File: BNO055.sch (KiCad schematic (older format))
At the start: 13 parts, among them SW2 SW_Push, U3 BNO055, Y2 32.768kHz

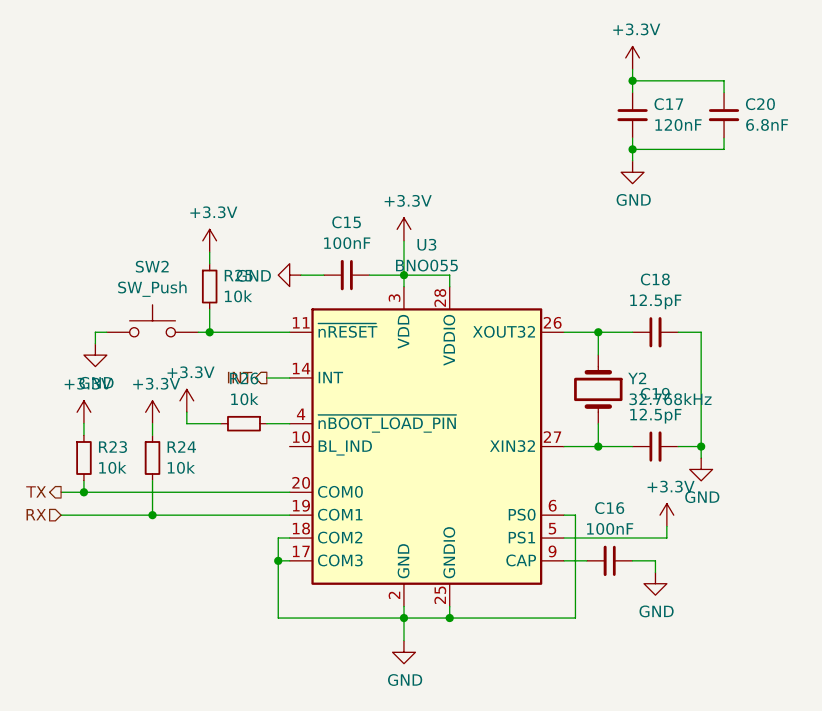
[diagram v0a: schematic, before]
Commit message: LMZM23600 from official kicad lib
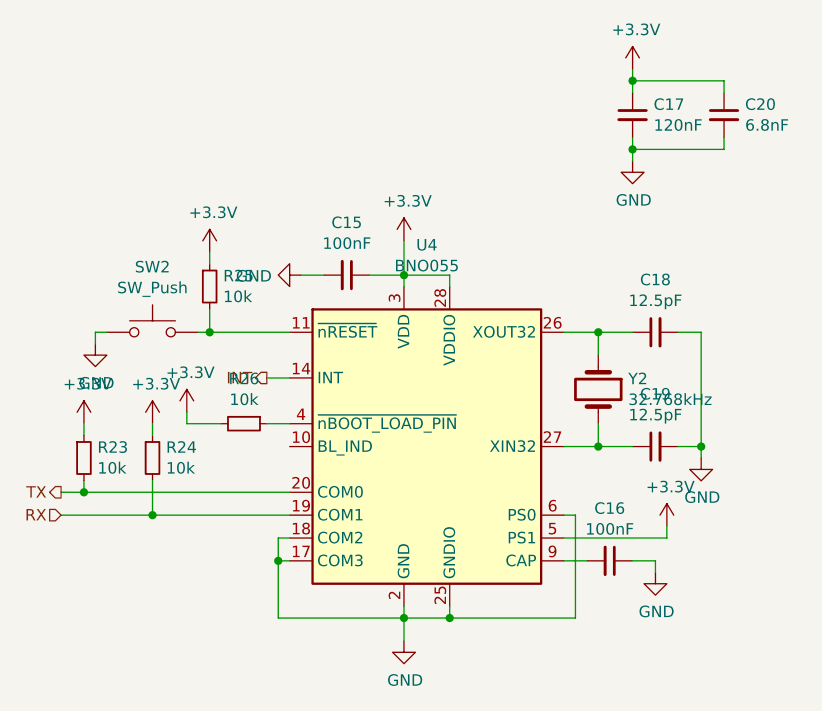
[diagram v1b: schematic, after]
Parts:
- renumbered U3 to U4
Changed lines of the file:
@@
 $EndDescr
 $Comp
-L Sensor_Motion:BNO055 U3
+L Sensor_Motion:BNO055 U4
 U 1 1 5C912A06
 P 6050 3250
-F 0 "U3" H 6050 4131 50  0000 C CNN
+F 0 "U4" H 6050 4131 50  0000 C CNN
 F 1 "BNO055" H 6050 4040 50  0000 C CNN
 F 2 "Package_LGA:LGA-28_5.2x3.8mm_P0.5mm" H 6300 2600 50  0001 L CNN

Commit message: use submodule for FT230
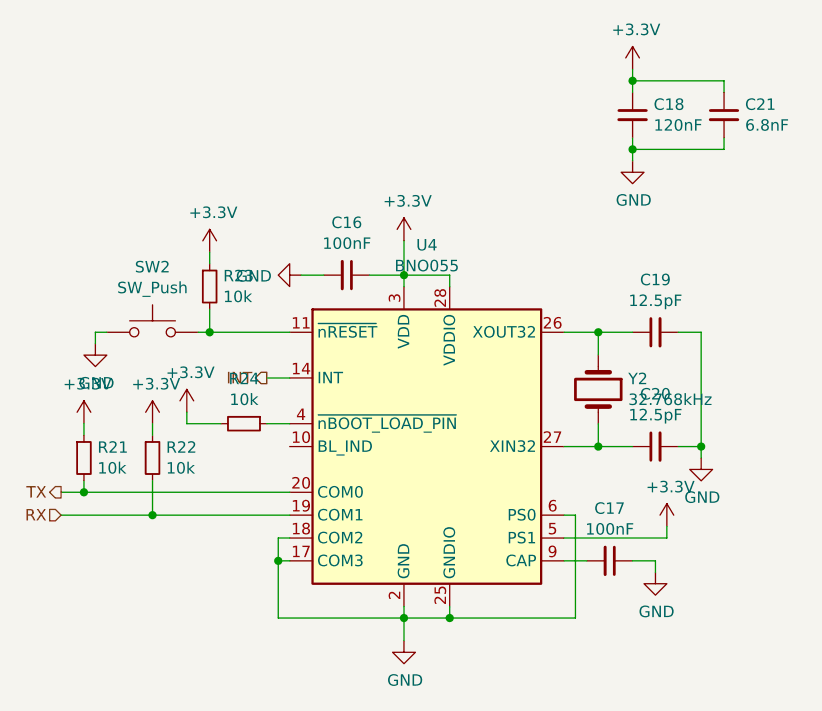
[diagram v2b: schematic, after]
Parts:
- renumbered C15 to C16, C16 to C17, C17 to C18, C18 to C19, C19 to C20, C20 to C21, R23 to R21, R24 to R22, R25 to R23, R26 to R24
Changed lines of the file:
@@
 	5950 4000 5950 4100
 $Comp
-L Device:R_Small R26
+L Device:R_Small R24
 U 1 1 5C915151
 P 5250 3150
-F 0 "R26" V 5054 3150 50  0000 C CNN
+F 0 "R24" V 5054 3150 50  0000 C CNN
 F 1 "10k" V 5145 3150 50  0000 C CNN
 F 2 "Resistor_SMD:R_0603_1608Metric" H 5250 3150 50  0001 C CNN
@@
 	6650 3750 6750 3750
 $Comp
-L Device:C_Small C16
+L Device:C_Small C17
 U 1 1 5C917F1C
 P 6850 3750
-F 0 "C16" V 6621 3750 50  0000 C CNN
+F 0 "C17" V 6621 3750 50  0000 C CNN
 F 1 "100nF" V 6712 3750 50  0000 C CNN
 F 2 "Capacitor_SMD:C_0603_1608Metric" H 6850 3750 50  0001 C CNN
@@
 $EndComp
 $Comp
-L Device:C_Small C15
+L Device:C_Small C16
 U 1 1 5C9184D6
 P 5700 2500
-F 0 "C15" V 5471 2500 50  0000 C CNN
+F 0 "C16" V 5471 2500 50  0000 C CNN
 F 1 "100nF" V 5562 2500 50  0000 C CNN
 F 2 "Capacitor_SMD:C_0603_1608Metric" H 5700 2500 50  0001 C CNN
@@
 $EndComp
 $Comp
-L Device:C_Small C17
+L Device:C_Small C18
 U 1 1 5C9161DD
 P 6950 1800
-F 0 "C17" H 7042 1846 50  0000 L CNN
+F 0 "C18" H 7042 1846 50  0000 L CNN
 F 1 "120nF" H 7042 1755 50  0000 L CNN
 F 2 "Capacitor_SMD:C_0603_1608Metric" H 6950 1800 50  0001 C CNN
@@
 $EndComp
 $Comp
-L Device:C_Small C20
+L Device:C_Small C21
 U 1 1 5C91667F
 P 7350 1800
-F 0 "C20" H 7442 1846 50  0000 L CNN
+F 0 "C21" H 7442 1846 50  0000 L CNN
 F 1 "6.8nF" H 7442 1755 50  0000 L CNN
 F 2 "Capacitor_SMD:C_0603_1608Metric" H 7350 1800 50  0001 C CNN
@@
 Connection ~ 6800 2750
 $Comp
-L Device:C_Small C18
+L Device:C_Small C19
 U 1 1 5C91C8F7
 P 7050 2750
-F 0 "C18" V 7279 2750 50  0000 C CNN
+F 0 "C19" V 7279 2750 50  0000 C CNN
 F 1 "12.5pF" V 7188 2750 50  0000 C CNN
 F 2 "Capacitor_SMD:C_0603_1608Metric" H 7050 2750 50  0001 C CNN
@@
 $EndComp
 $Comp
-L Device:C_Small C19
+L Device:C_Small C20
 U 1 1 5C91D1A5
 P 7050 3250
-F 0 "C19" V 7279 3250 50  0000 C CNN
+F 0 "C20" V 7279 3250 50  0000 C CNN
 F 1 "12.5pF" V 7188 3250 50  0000 C CNN
 F 2 "Capacitor_SMD:C_0603_1608Metric" H 7050 3250 50  0001 C CNN
@@
 	5050 2750 5100 2750
 $Comp
-L Device:R_Small R25
+L Device:R_Small R23
 U 1 1 5C99602E
 P 5100 2550
-F 0 "R25" H 5159 2596 50  0000 L CNN
+F 0 "R23" H 5159 2596 50  0000 L CNN
 F 1 "10k" H 5159 2505 50  0000 L CNN
 F 2 "Resistor_SMD:R_0603_1608Metric" H 5100 2550 50  0001 C CNN
@@
 $EndComp
 $Comp
-L Device:R_Small R24
+L Device:R_Small R22
 U 1 1 5C987F45
 P 4850 3300
-F 0 "R24" H 4909 3346 50  0000 L CNN
+F 0 "R22" H 4909 3346 50  0000 L CNN
 F 1 "10k" H 4909 3255 50  0000 L CNN
 F 2 "Resistor_SMD:R_0603_1608Metric" H 4850 3300 50  0001 C CNN
@@
 $EndComp
 $Comp
-L Device:R_Small R23
+L Device:R_Small R21
 U 1 1 5C98871D
 P 4550 3300
-F 0 "R23" H 4609 3346 50  0000 L CNN
+F 0 "R21" H 4609 3346 50  0000 L CNN
 F 1 "10k" H 4609 3255 50  0000 L CNN
 F 2 "Resistor_SMD:R_0603_1608Metric" H 4550 3300 50  0001 C CNN

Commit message: pullups, jumpers
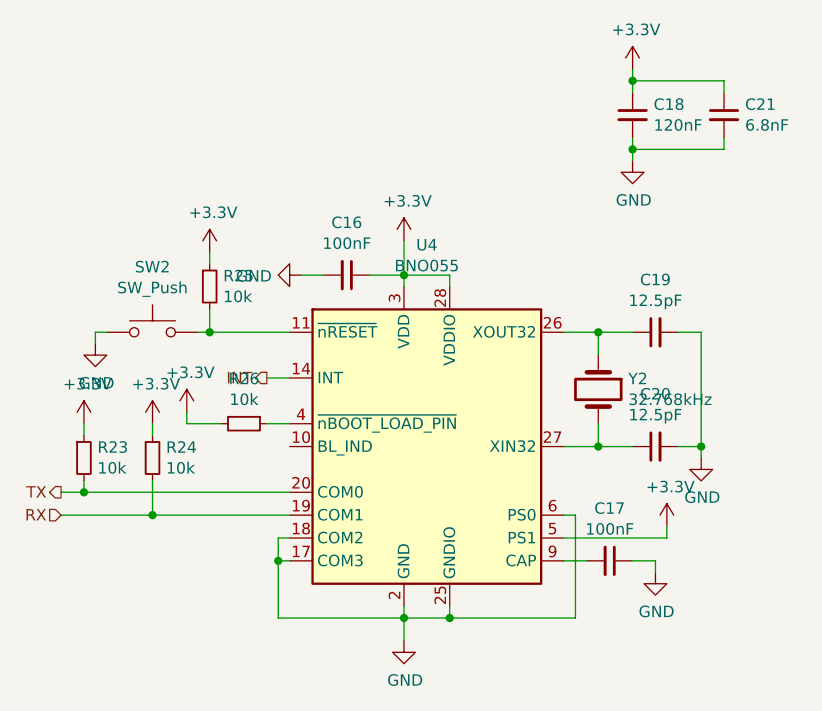
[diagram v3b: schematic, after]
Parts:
- renumbered R21 to R23, R22 to R24, R23 to R25, R24 to R26
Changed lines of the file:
@@
 	5950 4000 5950 4100
 $Comp
-L Device:R_Small R24
+L Device:R_Small R26
 U 1 1 5C915151
 P 5250 3150
-F 0 "R24" V 5054 3150 50  0000 C CNN
+F 0 "R26" V 5054 3150 50  0000 C CNN
 F 1 "10k" V 5145 3150 50  0000 C CNN
 F 2 "Resistor_SMD:R_0603_1608Metric" H 5250 3150 50  0001 C CNN
@@
 	5050 2750 5100 2750
 $Comp
-L Device:R_Small R23
+L Device:R_Small R25
 U 1 1 5C99602E
 P 5100 2550
-F 0 "R23" H 5159 2596 50  0000 L CNN
+F 0 "R25" H 5159 2596 50  0000 L CNN
 F 1 "10k" H 5159 2505 50  0000 L CNN
 F 2 "Resistor_SMD:R_0603_1608Metric" H 5100 2550 50  0001 C CNN
@@
 $EndComp
 $Comp
-L Device:R_Small R22
+L Device:R_Small R24
 U 1 1 5C987F45
 P 4850 3300
-F 0 "R22" H 4909 3346 50  0000 L CNN
+F 0 "R24" H 4909 3346 50  0000 L CNN
 F 1 "10k" H 4909 3255 50  0000 L CNN
 F 2 "Resistor_SMD:R_0603_1608Metric" H 4850 3300 50  0001 C CNN
@@
 $EndComp
 $Comp
-L Device:R_Small R21
+L Device:R_Small R23
 U 1 1 5C98871D
 P 4550 3300
-F 0 "R21" H 4609 3346 50  0000 L CNN
+F 0 "R23" H 4609 3346 50  0000 L CNN
 F 1 "10k" H 4609 3255 50  0000 L CNN
 F 2 "Resistor_SMD:R_0603_1608Metric" H 4550 3300 50  0001 C CNN

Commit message: layout
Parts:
- removed SW2: SW_Push, Button_Switch_SMD:SW_SPST_PTS810, symbol Switch:SW_Push
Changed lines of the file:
@@
 $EndComp
-$Comp
-L Switch:SW_Push SW?
-U 1 1 5C994ABC
-P 4850 2750
-AR Path="/5C8FB8FD/5C994ABC" Ref="SW?"  Part="1"
-AR Path="/5C9128F0/5C994ABC" Ref="SW2"  Part="1"
-F 0 "SW2" H 4850 3035 50  0000 C CNN
-F 1 "SW_Push" H 4850 2944 50  0000 C CNN
-F 2 "Button_Switch_SMD:SW_SPST_PTS810" H 4850 2950 50  0001 C CNN
-F 3 "~" H 4850 2950 50  0001 C CNN
-	1    4850 2750
-	1    0    0    -1
-$EndComp
-Wire Wire Line
-	4650 2750 4600 2750
-Wire Wire Line
-	4600 2750 4600 2800
-$Comp
-L power:GND #PWR?
-U 1 1 5C994AC5
-P 4600 2800
-AR Path="/5C8FB8FD/5C994AC5" Ref="#PWR?"  Part="1"
-AR Path="/5C9128F0/5C994AC5" Ref="#PWR043"  Part="1"
-F 0 "#PWR043" H 4600 2550 50  0001 C CNN
-F 1 "GND" H 4605 2627 50  0000 C CNN
-F 2 "" H 4600 2800 50  0001 C CNN
-F 3 "" H 4600 2800 50  0001 C CNN
-	1    4600 2800
-	1    0    0    -1
-$EndComp
-Wire Wire Line
-	5050 2750 5100 2750
 $Comp
 L Device:R_Small R25
@@
 Wire Wire Line
 	5100 2650 5100 2750
-Connection ~ 5100 2750
 Wire Wire Line
 	5100 2750 5450 2750

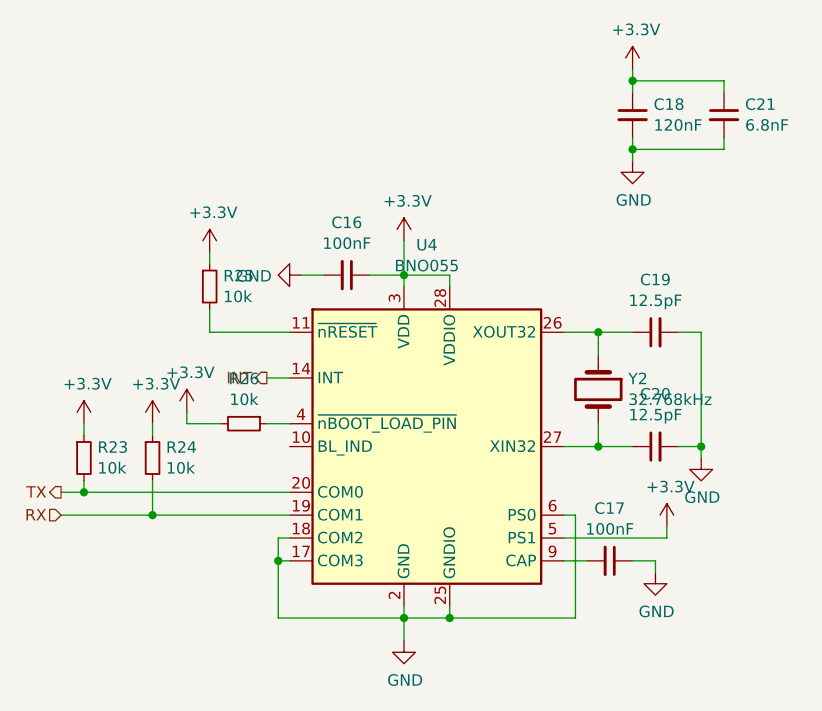
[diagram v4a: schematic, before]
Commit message: small layout fixes
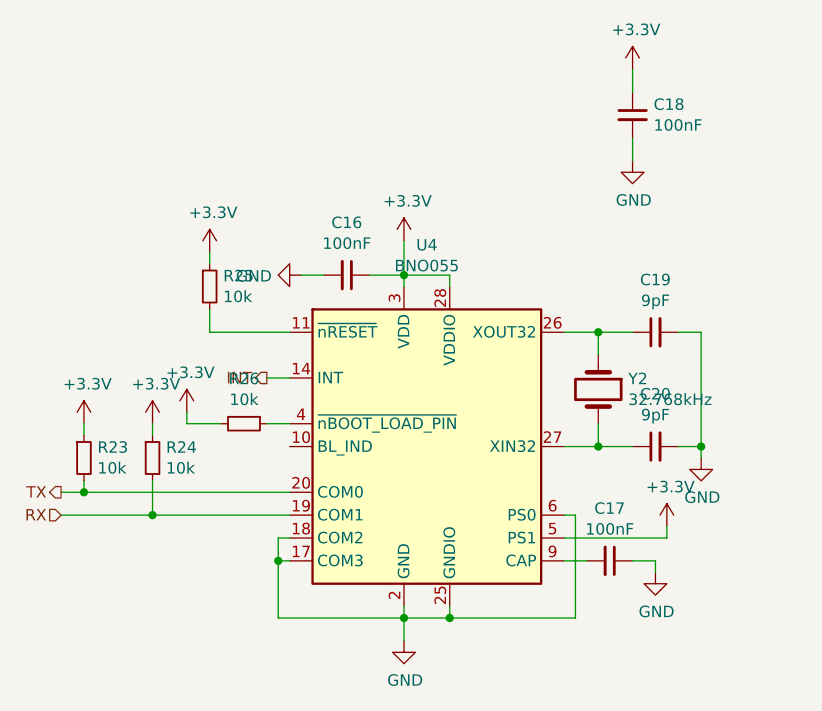
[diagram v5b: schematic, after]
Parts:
- removed C21: 6.8nF, Capacitor_SMD:C_0603_1608Metric, symbol Device:C_Small
- C18: value 120nF -> 100nF
- C19, C20: value 12.5pF -> 9pF
- Y2: MPN FC-135 32.7680KA-A5 -> FC-135 32.7680KA-AC0
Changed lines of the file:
@@
 P 6950 1800
 F 0 "C18" H 7042 1846 50  0000 L CNN
-F 1 "120nF" H 7042 1755 50  0000 L CNN
+F 1 "100nF" H 7042 1755 50  0000 L CNN
 F 2 "Capacitor_SMD:C_0603_1608Metric" H 6950 1800 50  0001 C CNN
 F 3 "~" H 6950 1800 50  0001 C CNN
@@
 	1    0    0    -1
 $EndComp
-$Comp
-L Device:C_Small C21
-U 1 1 5C91667F
-P 7350 1800
-F 0 "C21" H 7442 1846 50  0000 L CNN
-F 1 "6.8nF" H 7442 1755 50  0000 L CNN
-F 2 "Capacitor_SMD:C_0603_1608Metric" H 7350 1800 50  0001 C CNN
-F 3 "~" H 7350 1800 50  0001 C CNN
-	1    7350 1800
-	1    0    0    -1
-$EndComp
-Wire Wire Line
-	6950 1700 6950 1650
-Wire Wire Line
-	6950 1650 7350 1650
-Wire Wire Line
-	7350 1650 7350 1700
-Wire Wire Line
-	7350 1900 7350 1950
-Wire Wire Line
-	7350 1950 6950 1950
-Wire Wire Line
-	6950 1950 6950 1900
 $Comp
 L power:GND #PWR051
@@
 	1    0    0    -1
 $EndComp
-Wire Wire Line
-	6950 1600 6950 1650
-Connection ~ 6950 1650
-Wire Wire Line
-	6950 1950 6950 2000
-Connection ~ 6950 1950
 $Comp
 L Device:Crystal Y2
@@
 F 2 "Crystal:Crystal_SMD_3215-2Pin_3.2x1.5mm" H 6800 3000 50  0001 C CNN
 F 3 "~" H 6800 3000 50  0001 C CNN
-F 4 "FC-135 32.7680KA-A5" V 6800 3000 50  0001 C CNN "MPN"
+F 4 "FC-135 32.7680KA-AC0" V 6800 3000 50  0001 C CNN "MPN"
 	1    6800 3000
 	0    1    1    0
@@
 P 7050 2750
 F 0 "C19" V 7279 2750 50  0000 C CNN
-F 1 "12.5pF" V 7188 2750 50  0000 C CNN
+F 1 "9pF" V 7188 2750 50  0000 C CNN
 F 2 "Capacitor_SMD:C_0603_1608Metric" H 7050 2750 50  0001 C CNN
 F 3 "~" H 7050 2750 50  0001 C CNN
@@
 P 7050 3250
 F 0 "C20" V 7279 3250 50  0000 C CNN
-F 1 "12.5pF" V 7188 3250 50  0000 C CNN
+F 1 "9pF" V 7188 3250 50  0000 C CNN
 F 2 "Capacitor_SMD:C_0603_1608Metric" H 7050 3250 50  0001 C CNN
 F 3 "~" H 7050 3250 50  0001 C CNN
@@
 	1    0    0    -1
 $EndComp
+Wire Wire Line
+	6950 1600 6950 1700
+Wire Wire Line
+	6950 1900 6950 2000
 $EndSCHEMATC

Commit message: added NCs to satisfy ERC
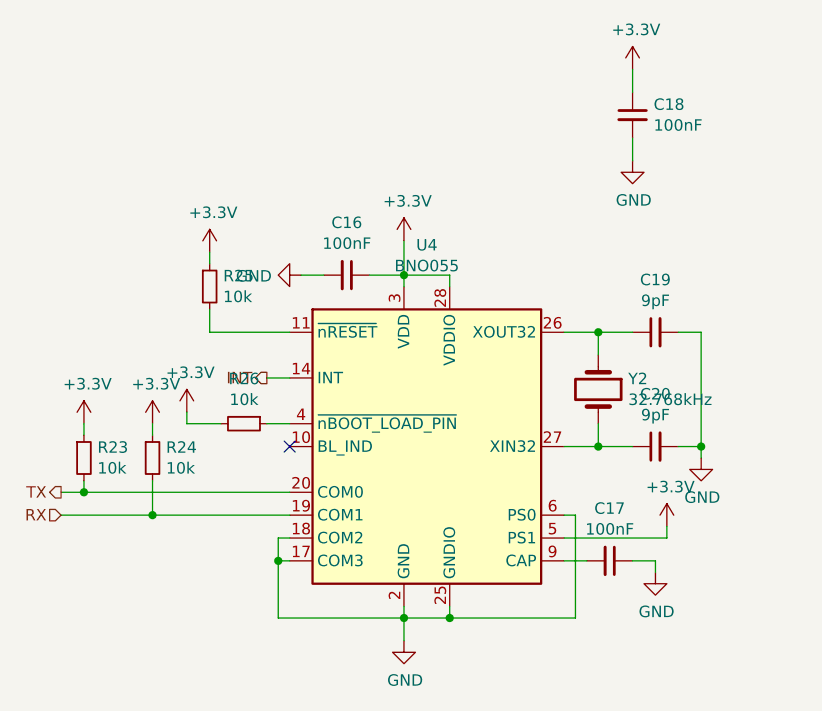
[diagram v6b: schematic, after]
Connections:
- no-connect marks 0 -> 1
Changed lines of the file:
@@
 Wire Wire Line
 	6950 1900 6950 2000
+NoConn ~ 5450 3250
 $EndSCHEMATC
